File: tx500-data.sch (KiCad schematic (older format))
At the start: 20 parts, among them U1 TUSB2036

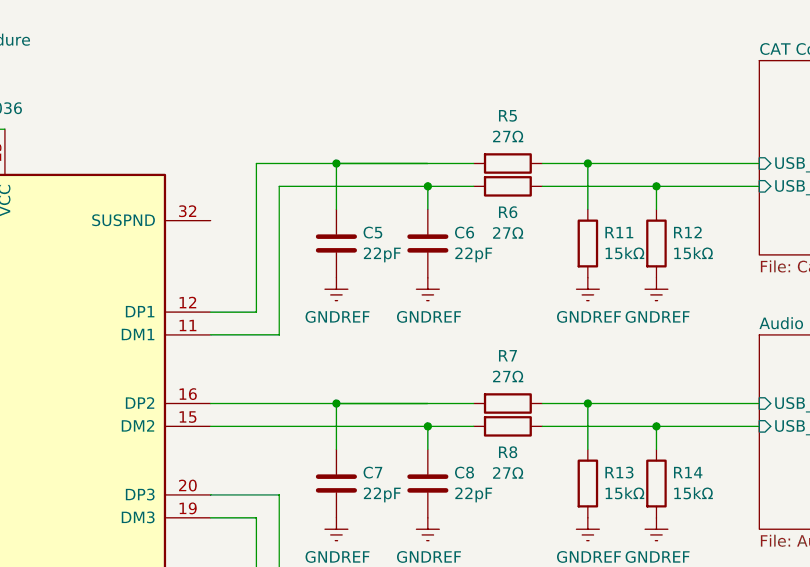
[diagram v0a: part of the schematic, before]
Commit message: Add a 15mm buffer for the GX12 bulkhead connectors
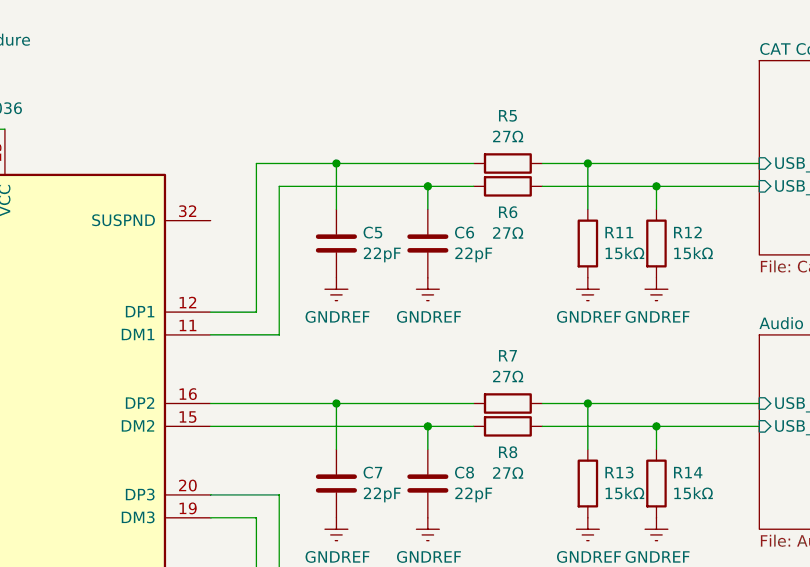
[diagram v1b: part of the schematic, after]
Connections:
- wire segments 73 -> 71

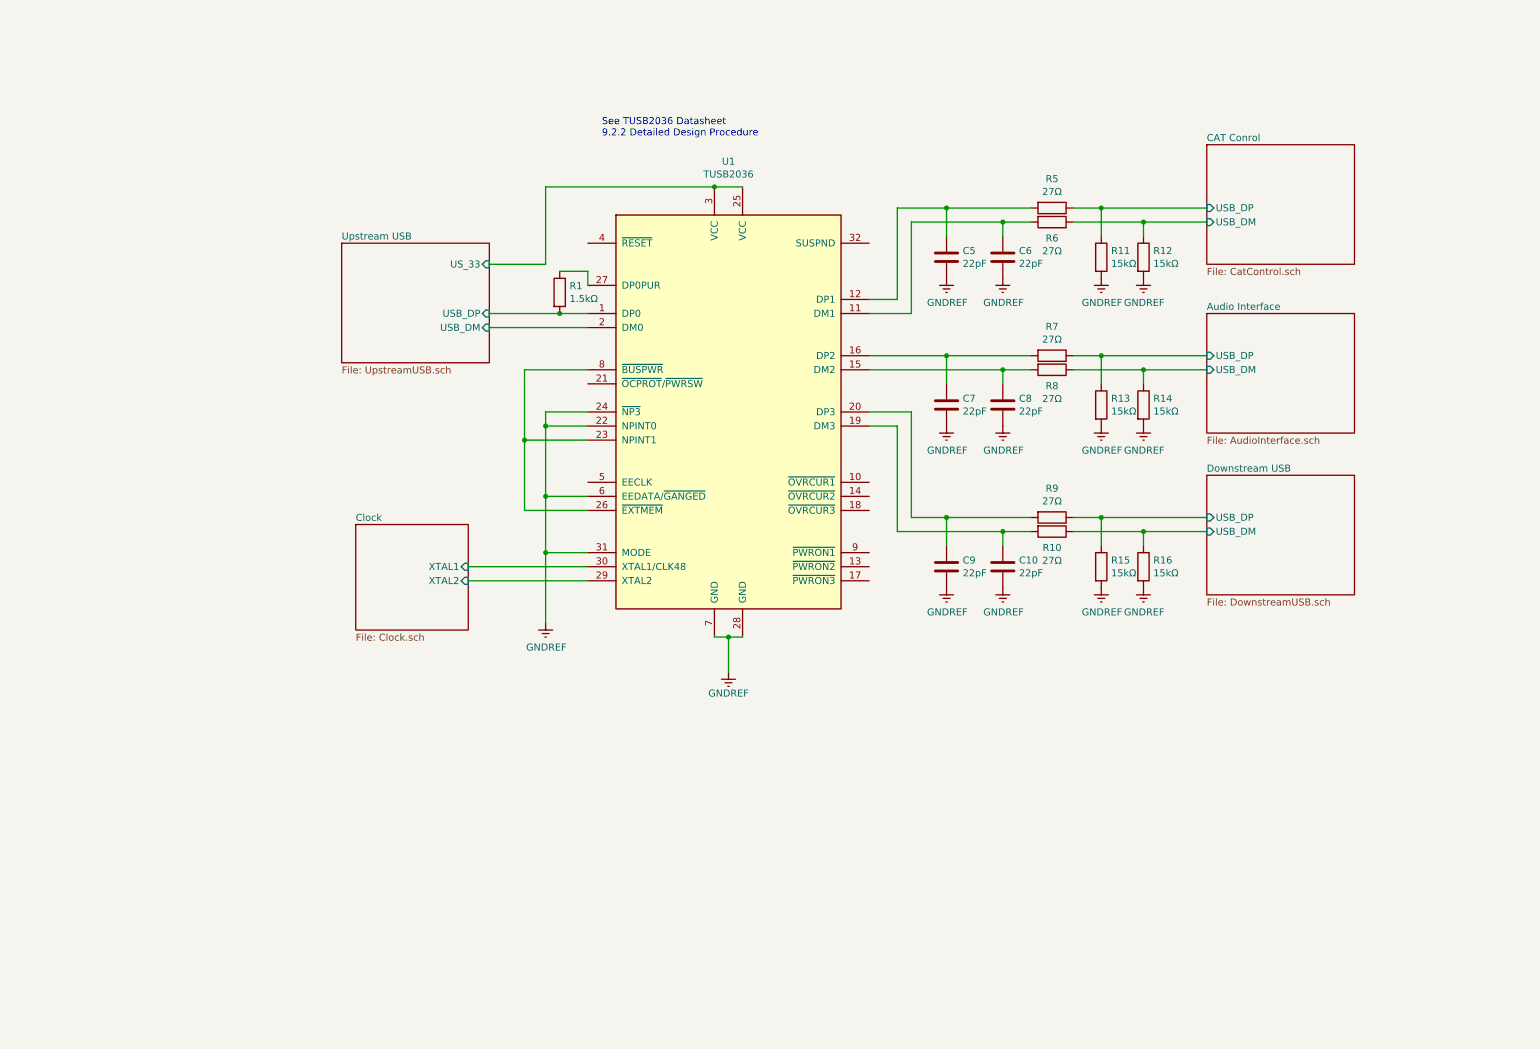
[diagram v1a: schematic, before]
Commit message: Add ID markings on schema and pcb
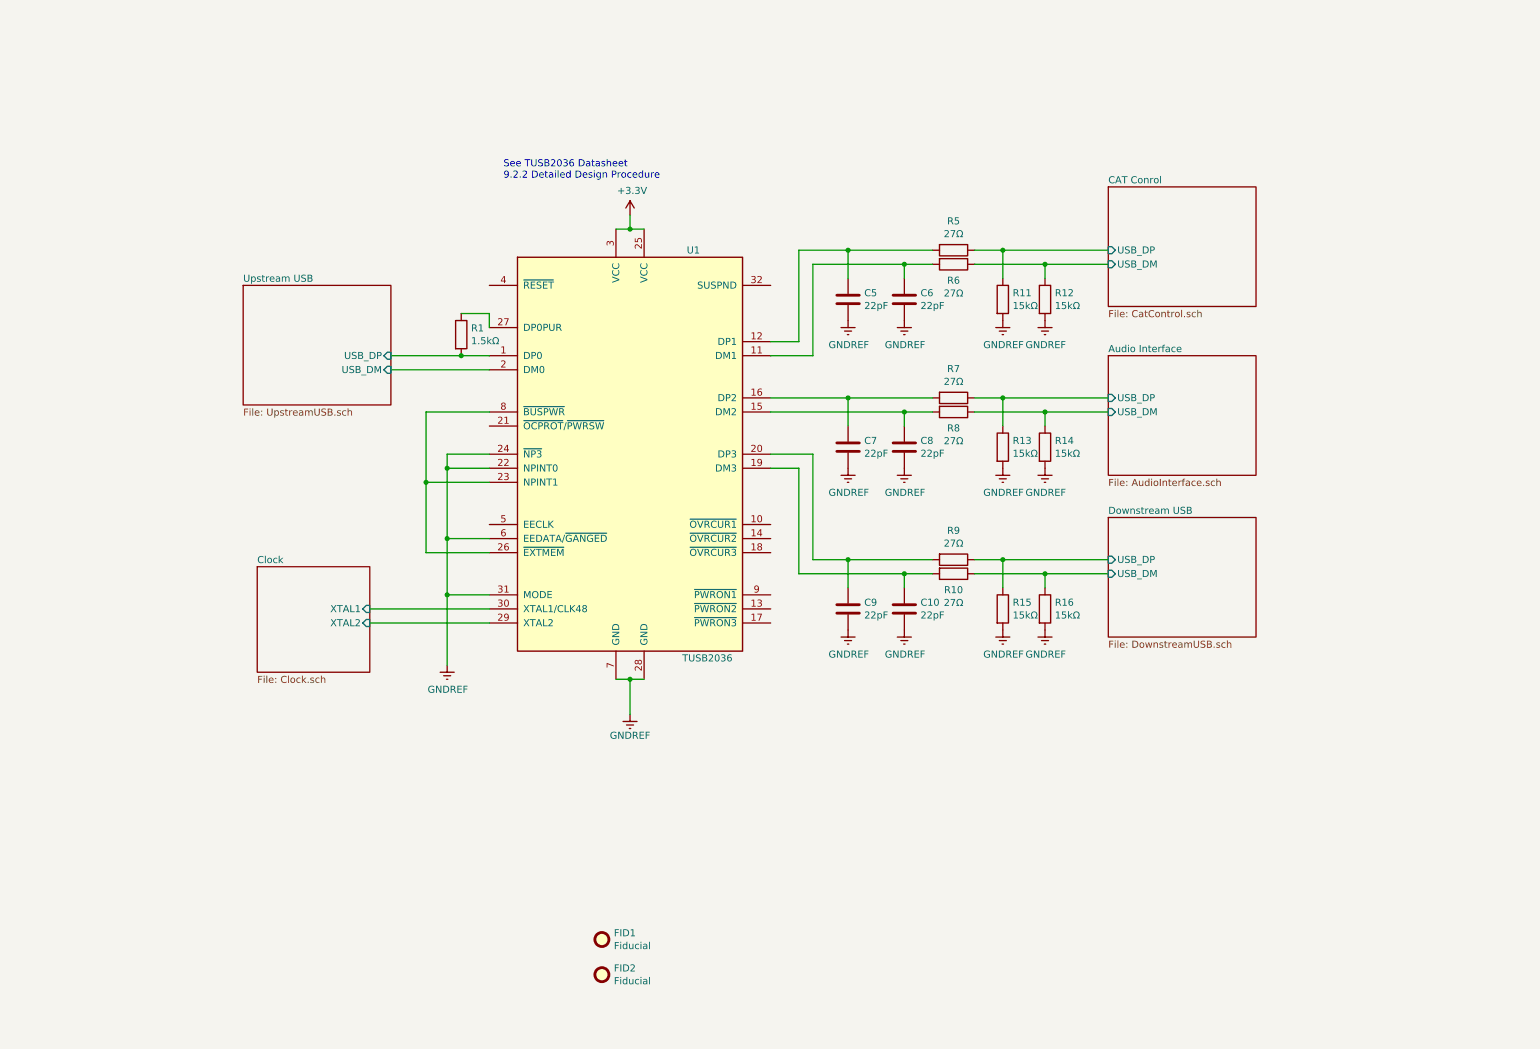
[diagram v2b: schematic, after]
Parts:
- added FID1, FID2: Fiducial, Fiducial:Fiducial_1mm_Mask2mm, symbol Mechanical:Fiducial
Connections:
- net Upstream USB/US_33 renamed +3V3
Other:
- moved on the sheet: C10, C5, C6, C7, C8, C9, R1, R10, R11, R12, R13, R14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

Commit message: First pass at routing PCB
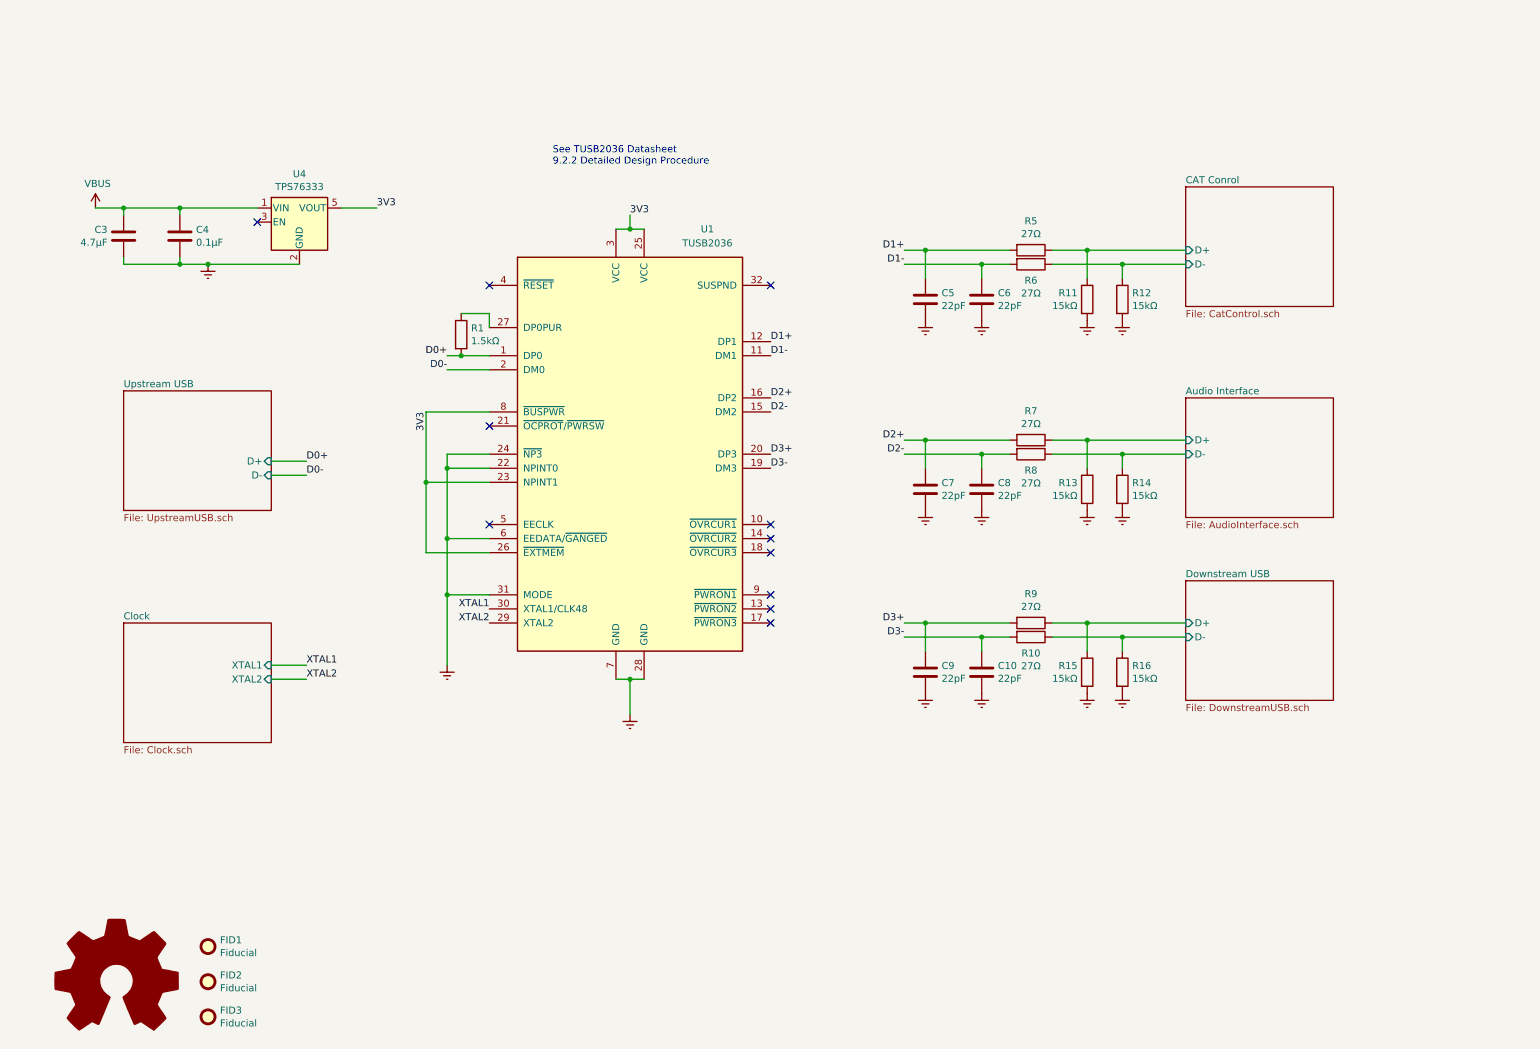
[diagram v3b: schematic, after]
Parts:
- added C3: 4.7μF, Capacitor_SMD:C_1210_3225Metric, symbol Device:C
- added C4: 0.1μF, Capacitor_SMD:C_1210_3225Metric, symbol Device:C
- added FID3: Fiducial, Fiducial:Fiducial_1mm_Mask2mm, symbol Mechanical:Fiducial
- added LOGO1: Logo_Open_Hardware_Large, Symbol:OSHW-Logo2_9.8x8mm_Copper, symbol Graphic:Logo_Open_Hardware_Large
- added U4: TPS76333, Package_TO_SOT_SMD:SOT-23-5, symbol Regulator_Linear:TPS76333
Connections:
- net +3V3 is gone; now on net 3V3: U1.25 (VCC), U1.3 (VCC)
- net GNDREF: now also C3.2, C4.2, U4.2 (GND)
- net D1-: now reaches C6.1, R6.2, U1.11 (DM1)
- net D1+: now reaches C5.1, R5.2, U1.12 (DP1)
- net D2-: now reaches C8.1, R8.2, U1.15 (DM2)
- net D2+: now reaches C7.1, R7.2, U1.16 (DP2)
- net D3-: now reaches C10.1, R10.2, U1.19 (DM3)
- net D3+: now reaches C9.1, R9.2, U1.20 (DP3)
- net 3V3: now reaches U1.23 (NPINT1), U1.26 (~EXTMEM), U1.8 (~BUSPWR)
- net 3V3: now also U4.5 (VOUT)
- net Audio Interface/USB_DM renamed Audio Interface/D-
- net Audio Interface/USB_DP renamed Audio Interface/D+
- net CAT Conrol/USB_DM renamed CAT Conrol/D-
- net CAT Conrol/USB_DP renamed CAT Conrol/D+
- net Clock/XTAL1 renamed XTAL1
- net Clock/XTAL2 renamed XTAL2
- net Downstream USB/USB_DM renamed Downstream USB/D-
- net Downstream USB/USB_DP renamed Downstream USB/D+
- net Upstream USB/USB_DM renamed D0-
- net Upstream USB/USB_DP renamed D0+
- new net VBUS: C3.1, C4.1, U4.1 (VIN)
- no-connect marks 0 -> 11
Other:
- moved on the sheet: C10, C5, C6, C7, C8, C9, FID1, FID2, R10, R11, R12, R13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

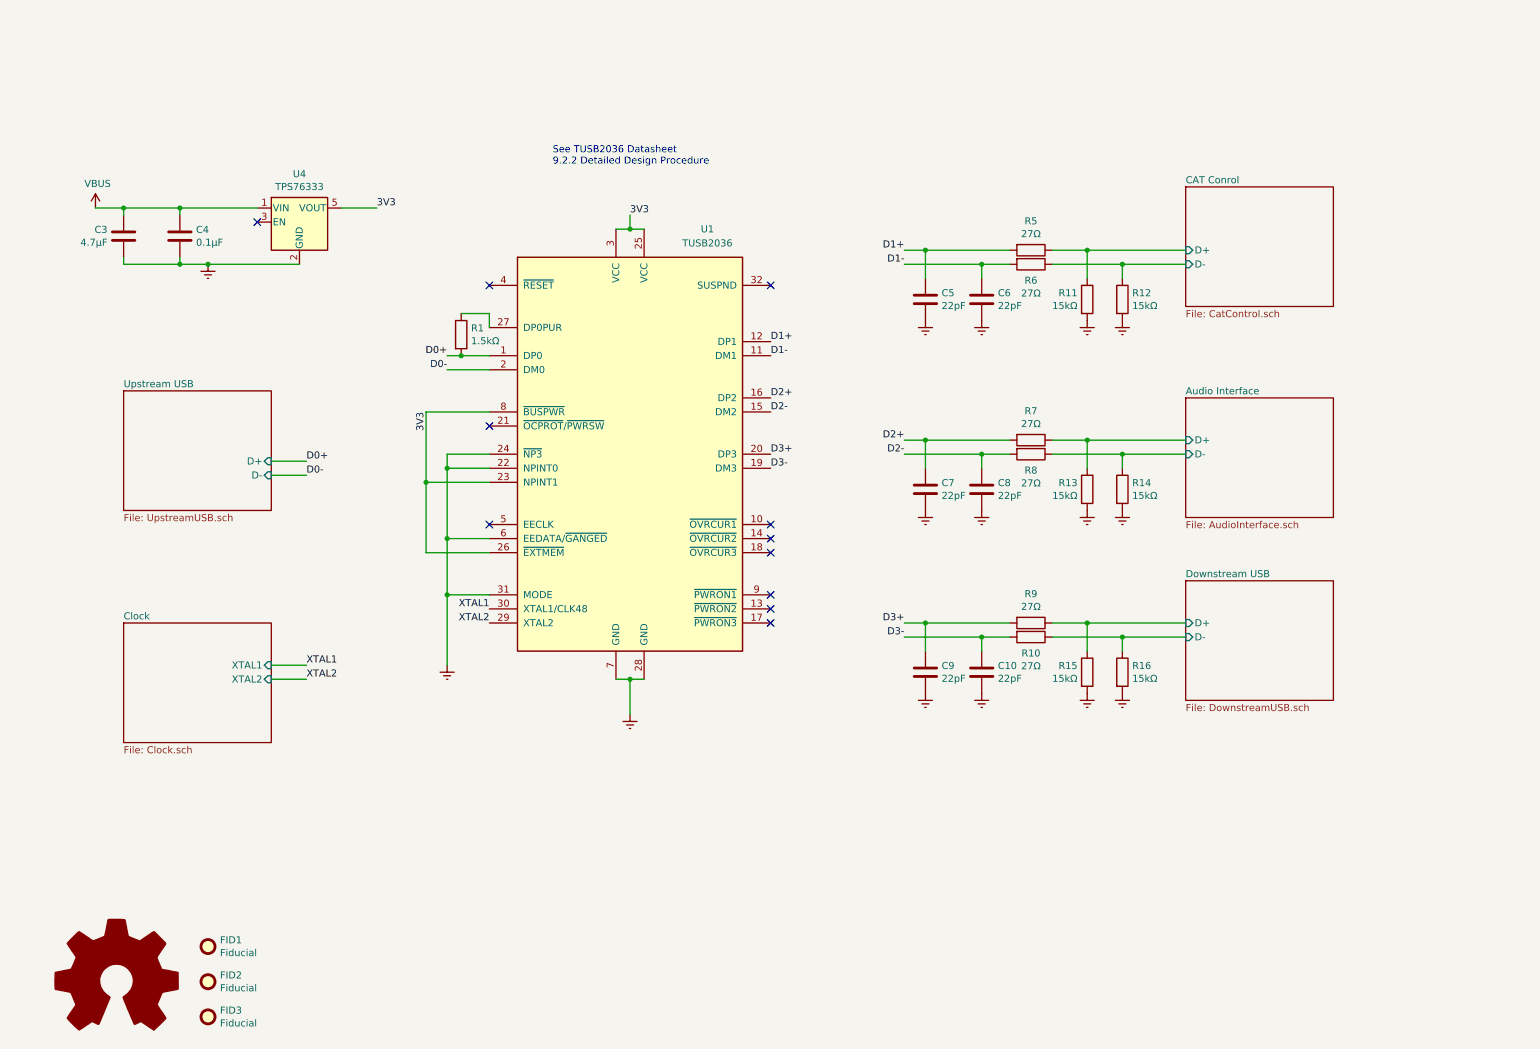
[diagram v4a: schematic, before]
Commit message: Reorganize onto one page
Suggested by eevblog.com/forum user teksturi, with thanks! https://www.eevblog.com/forum/oshw/advice-on-a-custom-usb-device/msg3518118/#msg3518118
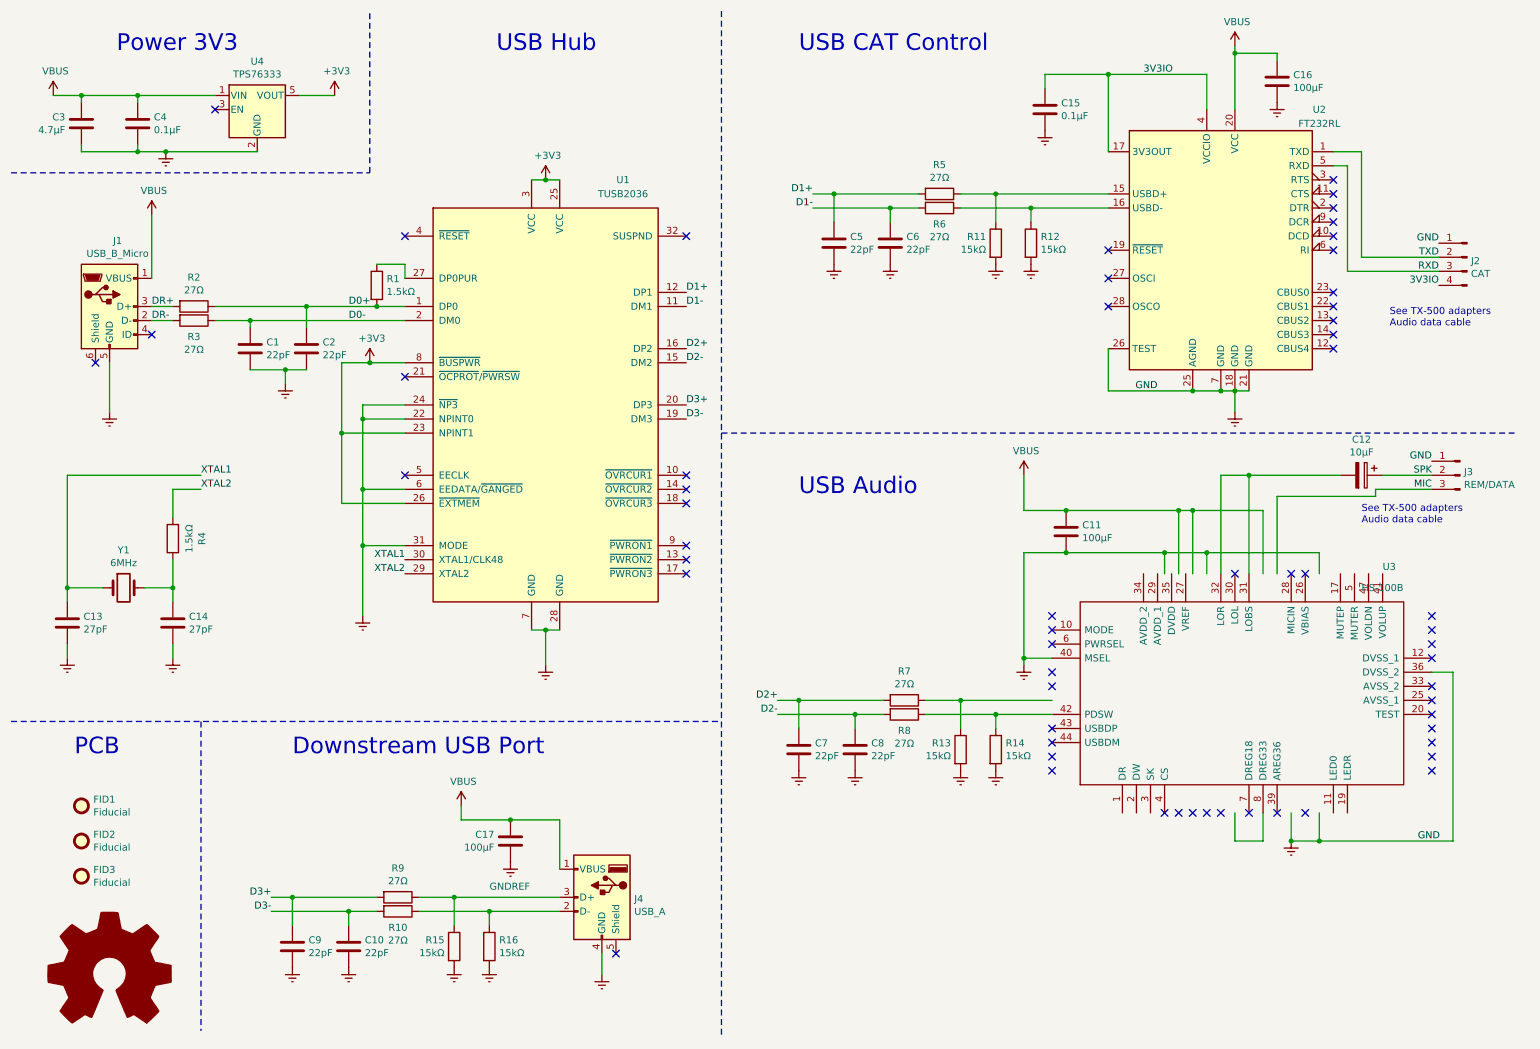
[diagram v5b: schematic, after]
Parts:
- added C1, C2: 22pF, Capacitor_SMD:C_1210_3225Metric, symbol Device:C
- added C11, C16, C17: 100μF, Capacitor_SMD:C_1210_3225Metric, symbol Device:C
- added C12: 10μF, Capacitor_SMD:C_1210_3225Metric, symbol Device:CP
- added C13, C14: 27pF, Capacitor_SMD:C_1210_3225Metric, symbol Device:C
- added C15: 0.1μF, Capacitor_SMD:C_1210_3225Metric, symbol Device:C
- added J1: USB_B_Micro, Connector_USB:USB_Micro-B_Molex_47346-0001, symbol Connector:USB_B_Micro
- added J2: CAT, Connector_JST:JST_PH_B4B-PH-SM4-TB_1x04-1MP_P2.00mm_Vertical, symbol Connector:Conn_01x04_Male
- added J3: REM/DATA, Connector_JST:JST_PH_B3B-PH-SM4-TB_1x03-1MP_P2.00mm_Vertical, symbol Connector:Conn_01x03_Male
- added J4: USB_A, Wurth-USBA:62900416021, symbol Connector:USB_A
- added R2, R3: 27Ω, Resistor_SMD:R_1210_3225Metric, symbol Device:R
- added R4: 1.5kΩ, Resistor_SMD:R_1210_3225Metric, symbol Device:R
- added U2: FT232RL, Package_SO:SSOP-28_5.3x10.2mm_P0.65mm, symbol Interface_USB:FT232RL
- added U3: HS-100B, Package_QFP:LQFP-48_7x7mm_P0.5mm, symbol HS-100B:HS-100B
- added Y1: 6MHz, Crystal:Crystal_SMD_Abracon_ABM7-2Pin_6.0x3.5mm, symbol Device:Crystal
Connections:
- net labels added: +3V3, 3V3IO, DR+, DR-, GND, MIC, RXD, SPK, TXD
- net labels removed: 3V3
- wire segments 75 -> 155
- no-connect marks 11 -> 59
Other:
- note added: "Downstream USB Port"
- note added: "PCB"
- note added: "Power 3V3"
- note added: "See TX-500 adapters\nAudio data cable"
- note added: "USB Audio"
- note added: "USB CAT Control"
- note added: "USB Hub"
- note removed: "See TUSB2036 Datasheet\n9.2.2 Detailed Design Procedure"
- moved on the sheet: C10, C3, C4, C5, C6, C7, C8, C9, FID1, FID2, FID3, R1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
